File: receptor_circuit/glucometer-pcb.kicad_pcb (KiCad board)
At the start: 2 copper layers, 36.9 x 68.2 mm, 21 parts

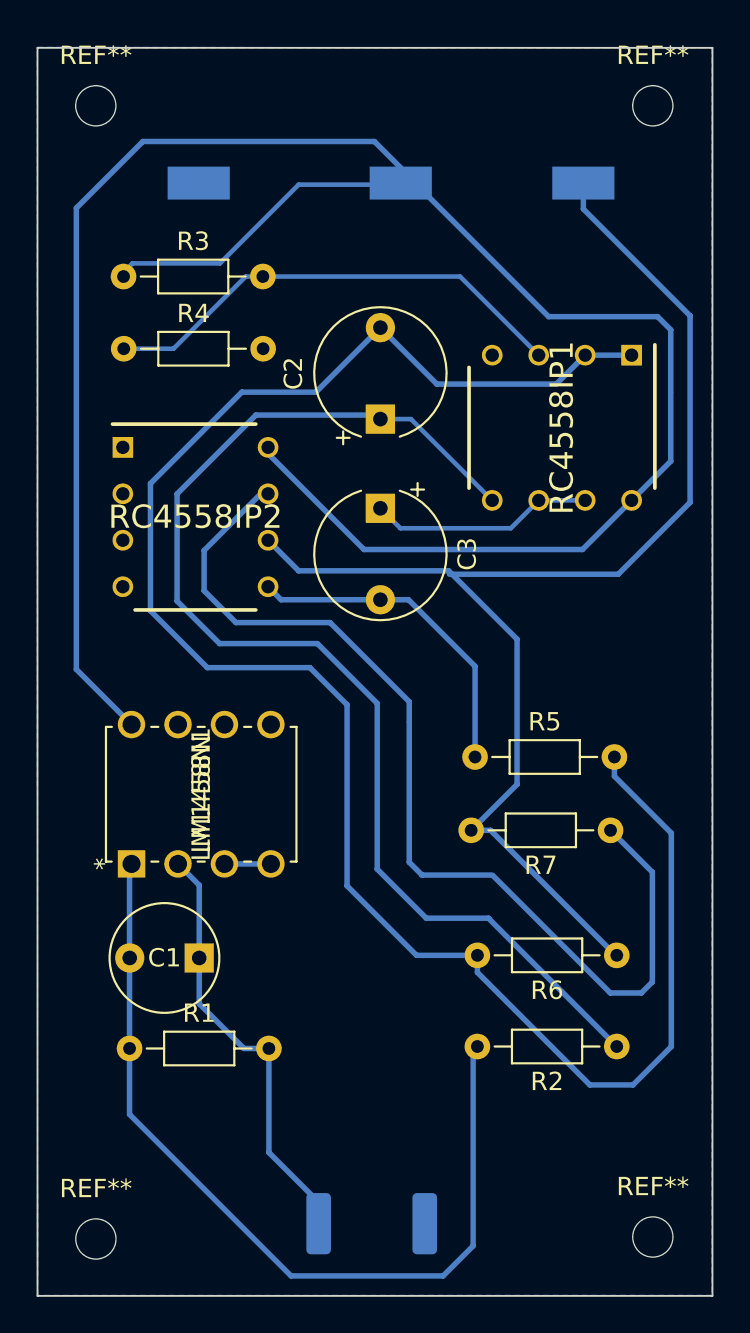
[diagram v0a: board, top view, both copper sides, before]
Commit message: updated footprints
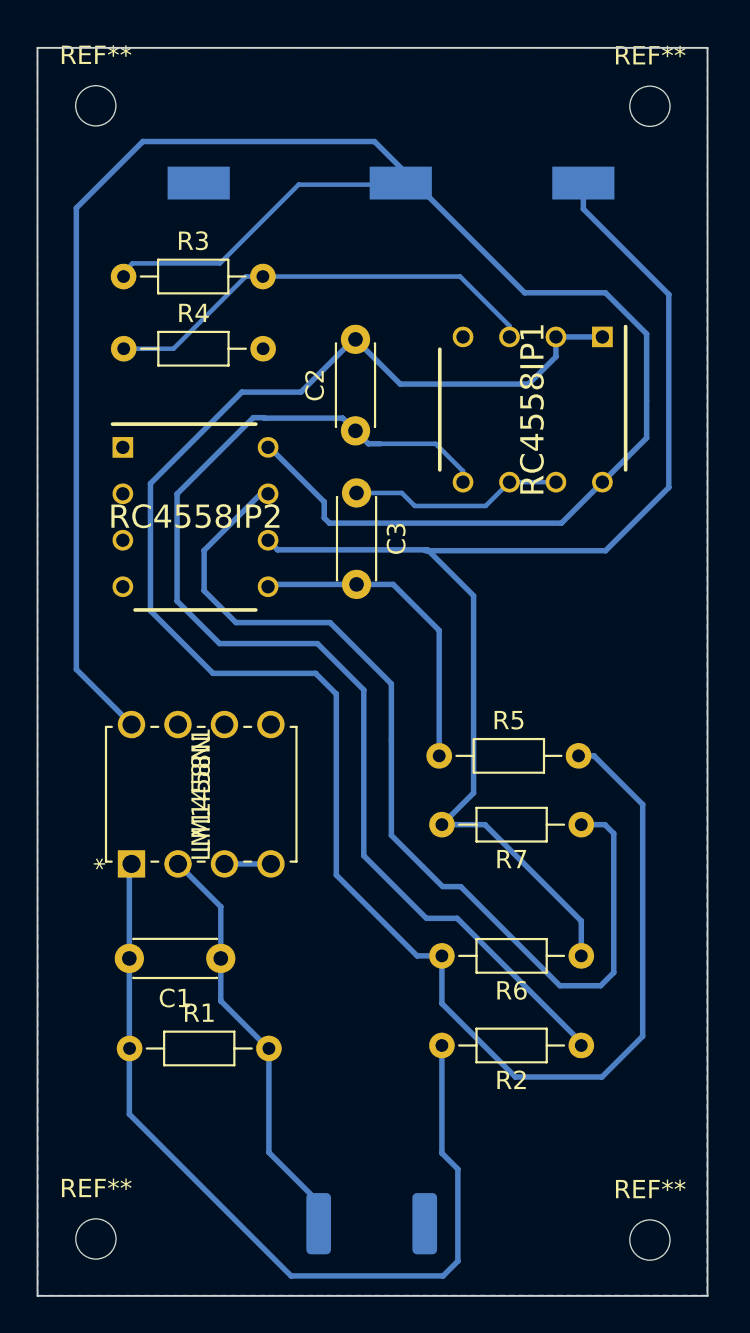
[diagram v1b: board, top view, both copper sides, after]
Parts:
- C1: footprint Capacitor_THT:CP_Radial_D8.0mm_P3.80mm -> Capacitor_THT:C_Disc_D4.3mm_W1.9mm_P5.00mm
- C2, C3: footprint Capacitor_THT:CP_Radial_Tantal_D7.0mm_P5.00mm -> Capacitor_THT:C_Disc_D4.3mm_W1.9mm_P5.00mm
- moved R5 1.96 mm to (194.6, 146.6)
- moved R6 1.94 mm to (202.4, 157.5)
- moved R2 1.94 mm to (202.4, 162.4)
- moved RC4558IP1 1.88 mm to (199.7, 127.7)
- moved R7 1.63 mm to (202.4, 150.4)
- moved C3 1.55 mm to (190.1, 132.2)
- moved C2 1.50 mm to (190.0, 128.8)
- moved C1 1.18 mm to (182.6, 157.7)
- moved REF** 0.23 mm to (206.1, 173.1)
- moved REF** 0.16 mm to (206.1, 111.1)
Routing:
- net VCC: track 119.3 -> 114.9 mm
- net /SIGNAL_1: track 66.4 -> 62.6 mm
- net Net-(R7-Pad1): track 55.5 -> 52.9 mm
- net Net-(R6-Pad1): track 72.7 -> 70.8 mm
- net /PWD_1.65: track 102.4 -> 100.6 mm
- net Net-(R3-Pad2): track 26.1 -> 24.4 mm
- net Net-(C1-Pad1): track 23.7 -> 22.9 mm
- net /SIGNAL_2: track 18.1 -> 17.3 mm
- net Net-(C3-Pad1): track 12.3 -> 11.7 mm
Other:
- board size 36.9 x 68.2 mm -> 36.6 x 68.2 mm

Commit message: updated pcbs
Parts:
- added C10: 15p, Capacitor_THT:C_Disc_D4.3mm_W1.9mm_P5.00mm, F.Cu at (178.8, 66.3)
- added C11: 100n, Capacitor_THT:C_Disc_D4.3mm_W1.9mm_P5.00mm, F.Cu at (186.2, 37.5)
- added C12: 10u, Capacitor_THT:C_Disc_D4.3mm_W1.9mm_P5.00mm, F.Cu at (186.3, 40.9)
- added C13: 15p, Capacitor_THT:C_Disc_D4.3mm_W1.9mm_P5.00mm, F.Cu at (228.8, 66.3)
- added C14: 100n, Capacitor_THT:C_Disc_D4.3mm_W1.9mm_P5.00mm, F.Cu at (236.2, 37.5)
- added C15: 10u, Capacitor_THT:C_Disc_D4.3mm_W1.9mm_P5.00mm, F.Cu at (236.3, 40.9)
- added C16: 15p, Capacitor_THT:C_Disc_D4.3mm_W1.9mm_P5.00mm, F.Cu at (28.8, 146.3)
- added C17: 100n, Capacitor_THT:C_Disc_D4.3mm_W1.9mm_P5.00mm, F.Cu at (36.2, 117.5)
- added C18: 10u, Capacitor_THT:C_Disc_D4.3mm_W1.9mm_P5.00mm, F.Cu at (36.3, 120.9)
- added C19: 15p, Capacitor_THT:C_Disc_D4.3mm_W1.9mm_P5.00mm, F.Cu at (78.8, 146.3)
- added C20: 100n, Capacitor_THT:C_Disc_D4.3mm_W1.9mm_P5.00mm, F.Cu at (86.2, 117.5)
- added C21: 10u, Capacitor_THT:C_Disc_D4.3mm_W1.9mm_P5.00mm, F.Cu at (86.3, 120.9)
- added C22: 15p, Capacitor_THT:C_Disc_D4.3mm_W1.9mm_P5.00mm, F.Cu at (128.8, 146.3)
- added C23: 100n, Capacitor_THT:C_Disc_D4.3mm_W1.9mm_P5.00mm, F.Cu at (136.2, 117.5)
- added C24: 10u, Capacitor_THT:C_Disc_D4.3mm_W1.9mm_P5.00mm, F.Cu at (136.3, 120.9)
- added C25: 15p, Capacitor_THT:C_Disc_D4.3mm_W1.9mm_P5.00mm, F.Cu at (178.8, 146.3)
- added C26: 100n, Capacitor_THT:C_Disc_D4.3mm_W1.9mm_P5.00mm, F.Cu at (186.2, 117.5)
- added C27: 10u, Capacitor_THT:C_Disc_D4.3mm_W1.9mm_P5.00mm, F.Cu at (186.3, 120.9)
- added C28: 15p, Capacitor_THT:C_Disc_D4.3mm_W1.9mm_P5.00mm, F.Cu at (228.8, 146.3)
- added C29: 100n, Capacitor_THT:C_Disc_D4.3mm_W1.9mm_P5.00mm, F.Cu at (236.2, 117.5)
- added C30: 10u, Capacitor_THT:C_Disc_D4.3mm_W1.9mm_P5.00mm, F.Cu at (236.3, 120.9)
- added C4: 15p, Capacitor_THT:C_Disc_D4.3mm_W1.9mm_P5.00mm, F.Cu at (78.8, 66.3)
- added C5: 100n, Capacitor_THT:C_Disc_D4.3mm_W1.9mm_P5.00mm, F.Cu at (86.2, 37.5)
- added C6: 10u, Capacitor_THT:C_Disc_D4.3mm_W1.9mm_P5.00mm, F.Cu at (86.3, 40.9)
- added C7: 15p, Capacitor_THT:C_Disc_D4.3mm_W1.9mm_P5.00mm, F.Cu at (128.8, 66.3)
- added C8: 100n, Capacitor_THT:C_Disc_D4.3mm_W1.9mm_P5.00mm, F.Cu at (136.2, 37.5)
- added C9: 10u, Capacitor_THT:C_Disc_D4.3mm_W1.9mm_P5.00mm, F.Cu at (136.3, 40.9)
- added GND10: TestPoint, TestPoint:TestPoint_Keystone_5015_Micro-Minature, B.Cu at (227.6, 103.9)
- added GND2: TestPoint, TestPoint:TestPoint_Keystone_5015_Micro-Minature, B.Cu at (77.6, 23.9)
- added GND3: TestPoint, TestPoint:TestPoint_Keystone_5015_Micro-Minature, B.Cu at (127.6, 23.9)
- added GND4: TestPoint, TestPoint:TestPoint_Keystone_5015_Micro-Minature, B.Cu at (177.6, 23.9)
- added GND5: TestPoint, TestPoint:TestPoint_Keystone_5015_Micro-Minature, B.Cu at (227.6, 23.9)
- added GND6: TestPoint, TestPoint:TestPoint_Keystone_5015_Micro-Minature, B.Cu at (27.6, 103.9)
- added GND7: TestPoint, TestPoint:TestPoint_Keystone_5015_Micro-Minature, B.Cu at (77.6, 103.9)
- added GND8: TestPoint, TestPoint:TestPoint_Keystone_5015_Micro-Minature, B.Cu at (127.6, 103.9)
- added GND9: TestPoint, TestPoint:TestPoint_Keystone_5015_Micro-Minature, B.Cu at (177.6, 103.9)
- added LM1458N10: LM1458N, Custom:MC1458N, F.Cu at (224.0, 141.1)
- added LM1458N2: LM1458N, Custom:MC1458N, F.Cu at (74.0, 61.1)
- added LM1458N3: LM1458N, Custom:MC1458N, F.Cu at (124.0, 61.1)
- added LM1458N4: LM1458N, Custom:MC1458N, F.Cu at (174.0, 61.1)
- added LM1458N5: LM1458N, Custom:MC1458N, F.Cu at (224.0, 61.1)
- added LM1458N6: LM1458N, Custom:MC1458N, F.Cu at (24.0, 141.1)
- added LM1458N7: LM1458N, Custom:MC1458N, F.Cu at (74.0, 141.1)
- added LM1458N8: LM1458N, Custom:MC1458N, F.Cu at (124.0, 141.1)
- added LM1458N9: LM1458N, Custom:MC1458N, F.Cu at (174.0, 141.1)
- added R10: 10k, Resistor_THT:R_Axial_DIN0204_L3.6mm_D1.6mm_P7.62mm_Horizontal, F.Cu at (73.5, 29.0)
- added R11: 10k, Resistor_THT:R_Axial_DIN0204_L3.6mm_D1.6mm_P7.62mm_Horizontal, F.Cu at (73.5, 33.0)
- added R12: 25k, Resistor_THT:R_Axial_DIN0204_L3.6mm_D1.6mm_P7.62mm_Horizontal, F.Cu at (90.8, 55.2)
- added R13: 1k, Resistor_THT:R_Axial_DIN0204_L3.6mm_D1.6mm_P7.62mm_Horizontal, F.Cu at (98.6, 66.2)
- added R14: 100k, Resistor_THT:R_Axial_DIN0204_L3.6mm_D1.6mm_P7.62mm_Horizontal, F.Cu at (98.6, 59.0)
- added R15: 100k, Resistor_THT:R_Axial_DIN0204_L3.6mm_D1.6mm_P7.62mm_Horizontal, F.Cu at (123.9, 71.2)
- added R16: 330k, Resistor_THT:R_Axial_DIN0204_L3.6mm_D1.6mm_P7.62mm_Horizontal, F.Cu at (148.6, 71.1)
- added R17: 10k, Resistor_THT:R_Axial_DIN0204_L3.6mm_D1.6mm_P7.62mm_Horizontal, F.Cu at (123.5, 29.0)
- added R18: 10k, Resistor_THT:R_Axial_DIN0204_L3.6mm_D1.6mm_P7.62mm_Horizontal, F.Cu at (123.5, 33.0)
- added R19: 25k, Resistor_THT:R_Axial_DIN0204_L3.6mm_D1.6mm_P7.62mm_Horizontal, F.Cu at (140.8, 55.2)
- added R20: 1k, Resistor_THT:R_Axial_DIN0204_L3.6mm_D1.6mm_P7.62mm_Horizontal, F.Cu at (148.6, 66.2)
- added R21: 100k, Resistor_THT:R_Axial_DIN0204_L3.6mm_D1.6mm_P7.62mm_Horizontal, F.Cu at (148.6, 59.0)
- added R22: 100k, Resistor_THT:R_Axial_DIN0204_L3.6mm_D1.6mm_P7.62mm_Horizontal, F.Cu at (173.9, 71.2)
- added R23: 330k, Resistor_THT:R_Axial_DIN0204_L3.6mm_D1.6mm_P7.62mm_Horizontal, F.Cu at (198.6, 71.1)
- added R24: 10k, Resistor_THT:R_Axial_DIN0204_L3.6mm_D1.6mm_P7.62mm_Horizontal, F.Cu at (173.5, 29.0)
- added R25: 10k, Resistor_THT:R_Axial_DIN0204_L3.6mm_D1.6mm_P7.62mm_Horizontal, F.Cu at (173.5, 33.0)
- added R26: 25k, Resistor_THT:R_Axial_DIN0204_L3.6mm_D1.6mm_P7.62mm_Horizontal, F.Cu at (190.8, 55.2)
- added R27: 1k, Resistor_THT:R_Axial_DIN0204_L3.6mm_D1.6mm_P7.62mm_Horizontal, F.Cu at (198.6, 66.2)
- added R28: 100k, Resistor_THT:R_Axial_DIN0204_L3.6mm_D1.6mm_P7.62mm_Horizontal, F.Cu at (198.6, 59.0)
- added R29: 100k, Resistor_THT:R_Axial_DIN0204_L3.6mm_D1.6mm_P7.62mm_Horizontal, F.Cu at (223.9, 71.2)
- added R30: 330k, Resistor_THT:R_Axial_DIN0204_L3.6mm_D1.6mm_P7.62mm_Horizontal, F.Cu at (248.6, 71.1)
- added R31: 10k, Resistor_THT:R_Axial_DIN0204_L3.6mm_D1.6mm_P7.62mm_Horizontal, F.Cu at (223.5, 29.0)
- added R32: 10k, Resistor_THT:R_Axial_DIN0204_L3.6mm_D1.6mm_P7.62mm_Horizontal, F.Cu at (223.5, 33.0)
- added R33: 25k, Resistor_THT:R_Axial_DIN0204_L3.6mm_D1.6mm_P7.62mm_Horizontal, F.Cu at (240.8, 55.2)
- added R34: 1k, Resistor_THT:R_Axial_DIN0204_L3.6mm_D1.6mm_P7.62mm_Horizontal, F.Cu at (248.6, 66.2)
- added R35: 100k, Resistor_THT:R_Axial_DIN0204_L3.6mm_D1.6mm_P7.62mm_Horizontal, F.Cu at (248.6, 59.0)
- added R36: 100k, Resistor_THT:R_Axial_DIN0204_L3.6mm_D1.6mm_P7.62mm_Horizontal, F.Cu at (23.9, 151.2)
- added R37: 330k, Resistor_THT:R_Axial_DIN0204_L3.6mm_D1.6mm_P7.62mm_Horizontal, F.Cu at (48.6, 151.1)
- added R38: 10k, Resistor_THT:R_Axial_DIN0204_L3.6mm_D1.6mm_P7.62mm_Horizontal, F.Cu at (23.5, 109.0)
- added R39: 10k, Resistor_THT:R_Axial_DIN0204_L3.6mm_D1.6mm_P7.62mm_Horizontal, F.Cu at (23.5, 113.0)
- added R40: 25k, Resistor_THT:R_Axial_DIN0204_L3.6mm_D1.6mm_P7.62mm_Horizontal, F.Cu at (40.8, 135.2)
- added R41: 1k, Resistor_THT:R_Axial_DIN0204_L3.6mm_D1.6mm_P7.62mm_Horizontal, F.Cu at (48.6, 146.2)
- added R42: 100k, Resistor_THT:R_Axial_DIN0204_L3.6mm_D1.6mm_P7.62mm_Horizontal, F.Cu at (48.6, 139.0)
- added R43: 100k, Resistor_THT:R_Axial_DIN0204_L3.6mm_D1.6mm_P7.62mm_Horizontal, F.Cu at (73.9, 151.2)
- added R44: 330k, Resistor_THT:R_Axial_DIN0204_L3.6mm_D1.6mm_P7.62mm_Horizontal, F.Cu at (98.6, 151.1)
- added R45: 10k, Resistor_THT:R_Axial_DIN0204_L3.6mm_D1.6mm_P7.62mm_Horizontal, F.Cu at (73.5, 109.0)
- added R46: 10k, Resistor_THT:R_Axial_DIN0204_L3.6mm_D1.6mm_P7.62mm_Horizontal, F.Cu at (73.5, 113.0)
- added R47: 25k, Resistor_THT:R_Axial_DIN0204_L3.6mm_D1.6mm_P7.62mm_Horizontal, F.Cu at (90.8, 135.2)
- added R48: 1k, Resistor_THT:R_Axial_DIN0204_L3.6mm_D1.6mm_P7.62mm_Horizontal, F.Cu at (98.6, 146.2)
- added R49: 100k, Resistor_THT:R_Axial_DIN0204_L3.6mm_D1.6mm_P7.62mm_Horizontal, F.Cu at (98.6, 139.0)
- added R50: 100k, Resistor_THT:R_Axial_DIN0204_L3.6mm_D1.6mm_P7.62mm_Horizontal, F.Cu at (123.9, 151.2)
- added R51: 330k, Resistor_THT:R_Axial_DIN0204_L3.6mm_D1.6mm_P7.62mm_Horizontal, F.Cu at (148.6, 151.1)
- added R52: 10k, Resistor_THT:R_Axial_DIN0204_L3.6mm_D1.6mm_P7.62mm_Horizontal, F.Cu at (123.5, 109.0)
- added R53: 10k, Resistor_THT:R_Axial_DIN0204_L3.6mm_D1.6mm_P7.62mm_Horizontal, F.Cu at (123.5, 113.0)
- added R54: 25k, Resistor_THT:R_Axial_DIN0204_L3.6mm_D1.6mm_P7.62mm_Horizontal, F.Cu at (140.8, 135.2)
- added R55: 1k, Resistor_THT:R_Axial_DIN0204_L3.6mm_D1.6mm_P7.62mm_Horizontal, F.Cu at (148.6, 146.2)
- added R56: 100k, Resistor_THT:R_Axial_DIN0204_L3.6mm_D1.6mm_P7.62mm_Horizontal, F.Cu at (148.6, 139.0)
- added R57: 100k, Resistor_THT:R_Axial_DIN0204_L3.6mm_D1.6mm_P7.62mm_Horizontal, F.Cu at (173.9, 151.2)
- added R58: 330k, Resistor_THT:R_Axial_DIN0204_L3.6mm_D1.6mm_P7.62mm_Horizontal, F.Cu at (198.6, 151.1)
- added R59: 10k, Resistor_THT:R_Axial_DIN0204_L3.6mm_D1.6mm_P7.62mm_Horizontal, F.Cu at (173.5, 109.0)
- added R60: 10k, Resistor_THT:R_Axial_DIN0204_L3.6mm_D1.6mm_P7.62mm_Horizontal, F.Cu at (173.5, 113.0)
- added R61: 25k, Resistor_THT:R_Axial_DIN0204_L3.6mm_D1.6mm_P7.62mm_Horizontal, F.Cu at (190.8, 135.2)
- added R62: 1k, Resistor_THT:R_Axial_DIN0204_L3.6mm_D1.6mm_P7.62mm_Horizontal, F.Cu at (198.6, 146.2)
- added R63: 100k, Resistor_THT:R_Axial_DIN0204_L3.6mm_D1.6mm_P7.62mm_Horizontal, F.Cu at (198.6, 139.0)
- added R64: 100k, Resistor_THT:R_Axial_DIN0204_L3.6mm_D1.6mm_P7.62mm_Horizontal, F.Cu at (223.9, 151.2)
- added R65: 330k, Resistor_THT:R_Axial_DIN0204_L3.6mm_D1.6mm_P7.62mm_Horizontal, F.Cu at (248.6, 151.1)
- added R66: 10k, Resistor_THT:R_Axial_DIN0204_L3.6mm_D1.6mm_P7.62mm_Horizontal, F.Cu at (223.5, 109.0)
- added R67: 10k, Resistor_THT:R_Axial_DIN0204_L3.6mm_D1.6mm_P7.62mm_Horizontal, F.Cu at (223.5, 113.0)
- added R68: 25k, Resistor_THT:R_Axial_DIN0204_L3.6mm_D1.6mm_P7.62mm_Horizontal, F.Cu at (240.8, 135.2)
- added R69: 1k, Resistor_THT:R_Axial_DIN0204_L3.6mm_D1.6mm_P7.62mm_Horizontal, F.Cu at (248.6, 146.2)
- added R70: 100k, Resistor_THT:R_Axial_DIN0204_L3.6mm_D1.6mm_P7.62mm_Horizontal, F.Cu at (248.6, 139.0)
- added R8: 100k, Resistor_THT:R_Axial_DIN0204_L3.6mm_D1.6mm_P7.62mm_Horizontal, F.Cu at (73.9, 71.2)
- added R9: 330k, Resistor_THT:R_Axial_DIN0204_L3.6mm_D1.6mm_P7.62mm_Horizontal, F.Cu at (98.6, 71.1)
- added RC4558IP10: RC4558IP, Custom:DIP794W53P254L959H508Q8N, F.Cu at (227.5, 42.2)
- added RC4558IP11: RC4558IP, Custom:DIP794W53P254L959H508Q8N, F.Cu at (45.9, 116.3)
- added RC4558IP12: RC4558IP, Custom:DIP794W53P254L959H508Q8N, F.Cu at (27.5, 122.2)
- added RC4558IP13: RC4558IP, Custom:DIP794W53P254L959H508Q8N, F.Cu at (95.9, 116.3)
- added RC4558IP14: RC4558IP, Custom:DIP794W53P254L959H508Q8N, F.Cu at (77.5, 122.2)
- added RC4558IP15: RC4558IP, Custom:DIP794W53P254L959H508Q8N, F.Cu at (145.9, 116.3)
- added RC4558IP16: RC4558IP, Custom:DIP794W53P254L959H508Q8N, F.Cu at (127.5, 122.2)
- added RC4558IP17: RC4558IP, Custom:DIP794W53P254L959H508Q8N, F.Cu at (195.9, 116.3)
- added RC4558IP18: RC4558IP, Custom:DIP794W53P254L959H508Q8N, F.Cu at (177.5, 122.2)
- added RC4558IP19: RC4558IP, Custom:DIP794W53P254L959H508Q8N, F.Cu at (245.9, 116.3)
- added RC4558IP20: RC4558IP, Custom:DIP794W53P254L959H508Q8N, F.Cu at (227.5, 122.2)
- added RC4558IP3: RC4558IP, Custom:DIP794W53P254L959H508Q8N, F.Cu at (95.9, 36.3)
- added RC4558IP4: RC4558IP, Custom:DIP794W53P254L959H508Q8N, F.Cu at (77.5, 42.2)
- added RC4558IP5: RC4558IP, Custom:DIP794W53P254L959H508Q8N, F.Cu at (145.9, 36.3)
- added RC4558IP6: RC4558IP, Custom:DIP794W53P254L959H508Q8N, F.Cu at (127.5, 42.2)
- added RC4558IP7: RC4558IP, Custom:DIP794W53P254L959H508Q8N, F.Cu at (195.9, 36.3)
- added RC4558IP8: RC4558IP, Custom:DIP794W53P254L959H508Q8N, F.Cu at (177.5, 42.2)
- added RC4558IP9: RC4558IP, Custom:DIP794W53P254L959H508Q8N, F.Cu at (245.9, 36.3)
- added RECEPTOR_DIODE10: D_Photo, LED_SMD:LED_2512_6332Metric, B.Cu at (237.1, 160.8)
- added RECEPTOR_DIODE2: D_Photo, LED_SMD:LED_2512_6332Metric, B.Cu at (87.1, 80.8)
- added RECEPTOR_DIODE3: D_Photo, LED_SMD:LED_2512_6332Metric, B.Cu at (137.1, 80.8)
- added RECEPTOR_DIODE4: D_Photo, LED_SMD:LED_2512_6332Metric, B.Cu at (187.1, 80.8)
- added RECEPTOR_DIODE5: D_Photo, LED_SMD:LED_2512_6332Metric, B.Cu at (237.1, 80.8)
- added RECEPTOR_DIODE6: D_Photo, LED_SMD:LED_2512_6332Metric, B.Cu at (37.1, 160.8)
- added RECEPTOR_DIODE7: D_Photo, LED_SMD:LED_2512_6332Metric, B.Cu at (87.1, 160.8)
- added RECEPTOR_DIODE8: D_Photo, LED_SMD:LED_2512_6332Metric, B.Cu at (137.1, 160.8)
- added RECEPTOR_DIODE9: D_Photo, LED_SMD:LED_2512_6332Metric, B.Cu at (187.1, 160.8)
- added REF**1: MountingHole_2.2mm_M2_ISO7380, MountingHole:MountingHole_2.2mm_M2_ISO7380, F.Cu at (102.3, 81.7)
- added REF**10: MountingHole_2.2mm_M2_ISO7380, MountingHole:MountingHole_2.2mm_M2_ISO7380, F.Cu at (172.0, 81.6)
- added REF**11: MountingHole_2.2mm_M2_ISO7380, MountingHole:MountingHole_2.2mm_M2_ISO7380, F.Cu at (202.3, 19.7)
- added REF**12: MountingHole_2.2mm_M2_ISO7380, MountingHole:MountingHole_2.2mm_M2_ISO7380, F.Cu at (172.0, 19.7)
- added REF**13: MountingHole_2.2mm_M2_ISO7380, MountingHole:MountingHole_2.2mm_M2_ISO7380, F.Cu at (252.3, 81.7)
- added REF**14: MountingHole_2.2mm_M2_ISO7380, MountingHole:MountingHole_2.2mm_M2_ISO7380, F.Cu at (222.0, 81.6)
- added REF**15: MountingHole_2.2mm_M2_ISO7380, MountingHole:MountingHole_2.2mm_M2_ISO7380, F.Cu at (252.3, 19.7)
- added REF**16: MountingHole_2.2mm_M2_ISO7380, MountingHole:MountingHole_2.2mm_M2_ISO7380, F.Cu at (222.0, 19.7)
- added REF**17: MountingHole_2.2mm_M2_ISO7380, MountingHole:MountingHole_2.2mm_M2_ISO7380, F.Cu at (52.3, 161.7)
- added REF**18: MountingHole_2.2mm_M2_ISO7380, MountingHole:MountingHole_2.2mm_M2_ISO7380, F.Cu at (22.0, 161.6)
- added REF**19: MountingHole_2.2mm_M2_ISO7380, MountingHole:MountingHole_2.2mm_M2_ISO7380, F.Cu at (52.3, 99.7)
- added REF**2: MountingHole_2.2mm_M2_ISO7380, MountingHole:MountingHole_2.2mm_M2_ISO7380, F.Cu at (72.0, 81.6)
- added REF**20: MountingHole_2.2mm_M2_ISO7380, MountingHole:MountingHole_2.2mm_M2_ISO7380, F.Cu at (22.0, 99.7)
- added REF**21: MountingHole_2.2mm_M2_ISO7380, MountingHole:MountingHole_2.2mm_M2_ISO7380, F.Cu at (102.3, 161.7)
- added REF**22: MountingHole_2.2mm_M2_ISO7380, MountingHole:MountingHole_2.2mm_M2_ISO7380, F.Cu at (72.0, 161.6)
- added REF**23: MountingHole_2.2mm_M2_ISO7380, MountingHole:MountingHole_2.2mm_M2_ISO7380, F.Cu at (102.3, 99.7)
- added REF**24: MountingHole_2.2mm_M2_ISO7380, MountingHole:MountingHole_2.2mm_M2_ISO7380, F.Cu at (72.0, 99.7)
- added REF**25: MountingHole_2.2mm_M2_ISO7380, MountingHole:MountingHole_2.2mm_M2_ISO7380, F.Cu at (152.3, 161.7)
- added REF**26: MountingHole_2.2mm_M2_ISO7380, MountingHole:MountingHole_2.2mm_M2_ISO7380, F.Cu at (122.0, 161.6)
- added REF**27: MountingHole_2.2mm_M2_ISO7380, MountingHole:MountingHole_2.2mm_M2_ISO7380, F.Cu at (152.3, 99.7)
- added REF**28: MountingHole_2.2mm_M2_ISO7380, MountingHole:MountingHole_2.2mm_M2_ISO7380, F.Cu at (122.0, 99.7)
- added REF**29: MountingHole_2.2mm_M2_ISO7380, MountingHole:MountingHole_2.2mm_M2_ISO7380, F.Cu at (202.3, 161.7)
- added REF**3: MountingHole_2.2mm_M2_ISO7380, MountingHole:MountingHole_2.2mm_M2_ISO7380, F.Cu at (102.3, 19.7)
- added REF**30: MountingHole_2.2mm_M2_ISO7380, MountingHole:MountingHole_2.2mm_M2_ISO7380, F.Cu at (172.0, 161.6)
- added REF**31: MountingHole_2.2mm_M2_ISO7380, MountingHole:MountingHole_2.2mm_M2_ISO7380, F.Cu at (202.3, 99.7)
- added REF**32: MountingHole_2.2mm_M2_ISO7380, MountingHole:MountingHole_2.2mm_M2_ISO7380, F.Cu at (172.0, 99.7)
- added REF**33: MountingHole_2.2mm_M2_ISO7380, MountingHole:MountingHole_2.2mm_M2_ISO7380, F.Cu at (252.3, 161.7)
- added REF**34: MountingHole_2.2mm_M2_ISO7380, MountingHole:MountingHole_2.2mm_M2_ISO7380, F.Cu at (222.0, 161.6)
- added REF**35: MountingHole_2.2mm_M2_ISO7380, MountingHole:MountingHole_2.2mm_M2_ISO7380, F.Cu at (252.3, 99.7)
- added REF**36: MountingHole_2.2mm_M2_ISO7380, MountingHole:MountingHole_2.2mm_M2_ISO7380, F.Cu at (222.0, 99.7)
- added REF**4: MountingHole_2.2mm_M2_ISO7380, MountingHole:MountingHole_2.2mm_M2_ISO7380, F.Cu at (72.0, 19.7)
- added REF**5: MountingHole_2.2mm_M2_ISO7380, MountingHole:MountingHole_2.2mm_M2_ISO7380, F.Cu at (152.3, 81.7)
- added REF**6: MountingHole_2.2mm_M2_ISO7380, MountingHole:MountingHole_2.2mm_M2_ISO7380, F.Cu at (122.0, 81.6)
- added REF**7: MountingHole_2.2mm_M2_ISO7380, MountingHole:MountingHole_2.2mm_M2_ISO7380, F.Cu at (152.3, 19.7)
- added REF**8: MountingHole_2.2mm_M2_ISO7380, MountingHole:MountingHole_2.2mm_M2_ISO7380, F.Cu at (122.0, 19.7)
- added REF**9: MountingHole_2.2mm_M2_ISO7380, MountingHole:MountingHole_2.2mm_M2_ISO7380, F.Cu at (202.3, 81.7)
- added S_OUT10: SIGNAL_OUT, TestPoint:TestPoint_Keystone_5015_Micro-Minature, B.Cu at (248.7, 103.9)
- added S_OUT2: SIGNAL_OUT, TestPoint:TestPoint_Keystone_5015_Micro-Minature, B.Cu at (98.7, 23.9)
- added S_OUT3: SIGNAL_OUT, TestPoint:TestPoint_Keystone_5015_Micro-Minature, B.Cu at (148.7, 23.9)
- added S_OUT4: SIGNAL_OUT, TestPoint:TestPoint_Keystone_5015_Micro-Minature, B.Cu at (198.7, 23.9)
- added S_OUT5: SIGNAL_OUT, TestPoint:TestPoint_Keystone_5015_Micro-Minature, B.Cu at (248.7, 23.9)
- added S_OUT6: SIGNAL_OUT, TestPoint:TestPoint_Keystone_5015_Micro-Minature, B.Cu at (48.7, 103.9)
- added S_OUT7: SIGNAL_OUT, TestPoint:TestPoint_Keystone_5015_Micro-Minature, B.Cu at (98.7, 103.9)
- added S_OUT8: SIGNAL_OUT, TestPoint:TestPoint_Keystone_5015_Micro-Minature, B.Cu at (148.7, 103.9)
- added S_OUT9: SIGNAL_OUT, TestPoint:TestPoint_Keystone_5015_Micro-Minature, B.Cu at (198.7, 103.9)
- added VCC10: TestPoint, TestPoint:TestPoint_Keystone_5015_Micro-Minature, B.Cu at (238.7, 103.9)
- added VCC2: TestPoint, TestPoint:TestPoint_Keystone_5015_Micro-Minature, B.Cu at (88.7, 23.9)
- added VCC3: TestPoint, TestPoint:TestPoint_Keystone_5015_Micro-Minature, B.Cu at (138.7, 23.9)
- added VCC4: TestPoint, TestPoint:TestPoint_Keystone_5015_Micro-Minature, B.Cu at (188.7, 23.9)
- added VCC5: TestPoint, TestPoint:TestPoint_Keystone_5015_Micro-Minature, B.Cu at (238.7, 23.9)
- added VCC6: TestPoint, TestPoint:TestPoint_Keystone_5015_Micro-Minature, B.Cu at (38.7, 103.9)
- added VCC7: TestPoint, TestPoint:TestPoint_Keystone_5015_Micro-Minature, B.Cu at (88.7, 103.9)
- added VCC8: TestPoint, TestPoint:TestPoint_Keystone_5015_Micro-Minature, B.Cu at (138.7, 103.9)
- added VCC9: TestPoint, TestPoint:TestPoint_Keystone_5015_Micro-Minature, B.Cu at (188.7, 103.9)
- moved R1 178.9 mm to (23.9, 71.2)
- moved VCC1 178.9 mm to (38.7, 23.9)
- moved C1 178.9 mm to (28.8, 66.3)
- moved C2 178.9 mm to (36.2, 37.5)
- moved C3 178.9 mm to (36.3, 40.9)
- moved GND1 178.9 mm to (27.6, 23.9)
- moved LM1458N1 178.9 mm to (24.0, 61.1)
- moved R2 178.9 mm to (48.6, 71.1)
- moved R3 178.9 mm to (23.5, 29.0)
- moved R4 178.9 mm to (23.5, 33.0)
- moved R5 178.9 mm to (40.8, 55.2)
- moved R6 178.9 mm to (48.6, 66.2)
- moved R7 178.9 mm to (48.6, 59.0)
- moved RC4558IP1 178.9 mm to (45.9, 36.3)
- moved RC4558IP2 178.9 mm to (27.5, 42.2)
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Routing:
- net VCC: track 114.9 -> 1149.3 mm
- net /PWD_1.65: track 100.6 -> 1006.4 mm
- net Net-(R6-Pad1): track 70.8 -> 707.6 mm
- net /SIGNAL_1: track 62.6 -> 625.7 mm
- net Net-(R7-Pad1): track 52.9 -> 529.2 mm
- net Net-(C1-Pad2): track 47.8 -> 478.5 mm
- net Net-(R3-Pad2): track 24.4 -> 244.5 mm
- net Net-(C1-Pad1): track 22.9 -> 228.7 mm
- net /SIGNAL_2: track 17.3 -> 173.1 mm
- net Net-(C3-Pad1): track 11.7 -> 117.4 mm
- net GND: track 3.16 -> 31.6 mm
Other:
- board size 36.6 x 68.2 mm -> 236.6 x 148.2 mm

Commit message: added prints
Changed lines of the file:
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@@
     (pad_to_mask_clearance 0)
     (pcbplotparams
-      (layerselection 0x00010fc_ffffffff)
+      (layerselection 0x0000000_fffffffe)
       (disableapertmacros false)
       (usegerberextensions false)
@@
       (svguseinch false)
       (svgprecision 6)
-      (excludeedgelayer true)
+      (excludeedgelayer false)
       (plotframeref false)
       (viasonmask false)
@@
       (dxfimperialunits true)
       (dxfusepcbnewfont true)
-      (psnegative false)
+      (psnegative true)
       (psa4output false)
-      (plotreference true)
-      (plotvalue true)
+      (plotreference false)
+      (plotvalue false)
       (plotinvisibletext false)
       (sketchpadsonfab false)
       (subtractmaskfromsilk false)
-      (outputformat 1)
+      (outputformat 4)
       (mirror false)
       (drillshape 1)
       (scaleselection 1)
-      (outputdirectory "")
+      (outputdirectory "../ready-to-print/")
     )
   )
@@
     (fp_line (start 3.15 1.6) (end -2.35 1.6) (layer "B.Fab") (width 0.1))
     (fp_line (start -3.15 -1.6) (end 3.15 -1.6) (layer "B.Fab") (width 0.1))
-    (pad "1" smd roundrect (at -2.9 0 180) (size 1.35 3.35) (layers "B.Cu" "B.Paste" "B.Mask") (roundrect_rratio 0.185185)
+    (pad "1" smd roundrect (at -2.9 0 180) (size 1.35 3.35) (layers "B.Cu" "B.Paste" "B.Mask") (roundrect_rratio 0.1851851852)
       (net 8 "GND") (pinfunction "K") (pintype "passive"))
-    (pad "2" smd roundrect (at 2.9 0 180) (size 1.35 3.35) (layers "B.Cu" "B.Paste" "B.Mask") (roundrect_rratio 0.185185)
+    (pad "2" smd roundrect (at 2.9 0 180) (size 1.35 3.35) (layers "B.Cu" "B.Paste" "B.Mask") (roundrect_rratio 0.1851851852)
       (net 1 "Net-(C1-Pad1)") (pinfunction "A") (pintype "passive"))
     (model "${KICAD6_3DMODEL_DIR}/LED_SMD.3dshapes/LED_2512_6332Metric.wrl"
@@
     (fp_line (start 3.15 1.6) (end -2.35 1.6) (layer "B.Fab") (width 0.1))
     (fp_line (start -3.15 -1.6) (end 3.15 -1.6) (layer "B.Fab") (width 0.1))
-    (pad "1" smd roundrect (at -2.9 0 180) (size 1.35 3.35) (layers "B.Cu" "B.Paste" "B.Mask") (roundrect_rratio 0.185185)
+    (pad "1" smd roundrect (at -2.9 0 180) (size 1.35 3.35) (layers "B.Cu" "B.Paste" "B.Mask") (roundrect_rratio 0.1851851852)
       (net 8 "GND") (pinfunction "K") (pintype "passive"))
-    (pad "2" smd roundrect (at 2.9 0 180) (size 1.35 3.35) (layers "B.Cu" "B.Paste" "B.Mask") (roundrect_rratio 0.185185)
+    (pad "2" smd roundrect (at 2.9 0 180) (size 1.35 3.35) (layers "B.Cu" "B.Paste" "B.Mask") (roundrect_rratio 0.1851851852)
       (net 1 "Net-(C1-Pad1)") (pinfunction "A") (pintype "passive"))
     (model "${KICAD6_3DMODEL_DIR}/LED_SMD.3dshapes/LED_2512_6332Metric.wrl"
@@
     (fp_line (start 3.15 -1.6) (end 3.15 1.6) (layer "B.Fab") (width 0.1))
     (fp_line (start -2.35 1.6) (end -3.15 0.8) (layer "B.Fab") (width 0.1))
-    (pad "1" smd roundrect (at -2.9 0 180) (size 1.35 3.35) (layers "B.Cu" "B.Paste" "B.Mask") (roundrect_rratio 0.185185)
+    (pad "1" smd roundrect (at -2.9 0 180) (size 1.35 3.35) (layers "B.Cu" "B.Paste" "B.Mask") (roundrect_rratio 0.1851851852)
       (net 8 "GND") (pinfunction "K") (pintype "passive"))
-    (pad "2" smd roundrect (at 2.9 0 180) (size 1.35 3.35) (layers "B.Cu" "B.Paste" "B.Mask") (roundrect_rratio 0.185185)
+    (pad "2" smd roundrect (at 2.9 0 180) (size 1.35 3.35) (layers "B.Cu" "B.Paste" "B.Mask") (roundrect_rratio 0.1851851852)
       (net 1 "Net-(C1-Pad1)") (pinfunction "A") (pintype "passive"))
     (model "${KICAD6_3DMODEL_DIR}/LED_SMD.3dshapes/LED_2512_6332Metric.wrl"
@@
     (fp_line (start -2.35 1.6) (end -3.15 0.8) (layer "B.Fab") (width 0.1))
     (fp_line (start 3.15 1.6) (end -2.35 1.6) (layer "B.Fab") (width 0.1))
-    (pad "1" smd roundrect (at -2.9 0 180) (size 1.35 3.35) (layers "B.Cu" "B.Paste" "B.Mask") (roundrect_rratio 0.185185)
+    (pad "1" smd roundrect (at -2.9 0 180) (size 1.35 3.35) (layers "B.Cu" "B.Paste" "B.Mask") (roundrect_rratio 0.1851851852)
       (net 8 "GND") (pinfunction "K") (pintype "passive"))
-    (pad "2" smd roundrect (at 2.9 0 180) (size 1.35 3.35) (layers "B.Cu" "B.Paste" "B.Mask") (roundrect_rratio 0.185185)
+    (pad "2" smd roundrect (at 2.9 0 180) (size 1.35 3.35) (layers "B.Cu" "B.Paste" "B.Mask") (roundrect_rratio 0.1851851852)
       (net 1 "Net-(C1-Pad1)") (pinfunction "A") (pintype "passive"))
     (model "${KICAD6_3DMODEL_DIR}/LED_SMD.3dshapes/LED_2512_6332Metric.wrl"
@@
     (fp_line (start -3.15 0.8) (end -3.15 -1.6) (layer "B.Fab") (width 0.1))
     (fp_line (start 3.15 -1.6) (end 3.15 1.6) (layer "B.Fab") (width 0.1))
-    (pad "1" smd roundrect (at -2.9 0 180) (size 1.35 3.35) (layers "B.Cu" "B.Paste" "B.Mask") (roundrect_rratio 0.185185)
+    (pad "1" smd roundrect (at -2.9 0 180) (size 1.35 3.35) (layers "B.Cu" "B.Paste" "B.Mask") (roundrect_rratio 0.1851851852)
       (net 8 "GND") (pinfunction "K") (pintype "passive"))
-    (pad "2" smd roundrect (at 2.9 0 180) (size 1.35 3.35) (layers "B.Cu" "B.Paste" "B.Mask") (roundrect_rratio 0.185185)
+    (pad "2" smd roundrect (at 2.9 0 180) (size 1.35 3.35) (layers "B.Cu" "B.Paste" "B.Mask") (roundrect_rratio 0.1851851852)
       (net 1 "Net-(C1-Pad1)") (pinfunction "A") (pintype "passive"))
     (model "${KICAD6_3DMODEL_DIR}/LED_SMD.3dshapes/LED_2512_6332Metric.wrl"
@@
     (fp_line (start -3.15 0.8) (end -3.15 -1.6) (layer "B.Fab") (width 0.1))
     (fp_line (start 3.15 -1.6) (end 3.15 1.6) (layer "B.Fab") (width 0.1))
-    (pad "1" smd roundrect (at -2.9 0 180) (size 1.35 3.35) (layers "B.Cu" "B.Paste" "B.Mask") (roundrect_rratio 0.185185)
+    (pad "1" smd roundrect (at -2.9 0 180) (size 1.35 3.35) (layers "B.Cu" "B.Paste" "B.Mask") (roundrect_rratio 0.1851851852)
       (net 8 "GND") (pinfunction "K") (pintype "passive"))
-    (pad "2" smd roundrect (at 2.9 0 180) (size 1.35 3.35) (layers "B.Cu" "B.Paste" "B.Mask") (roundrect_rratio 0.185185)
+    (pad "2" smd roundrect (at 2.9 0 180) (size 1.35 3.35) (layers "B.Cu" "B.Paste" "B.Mask") (roundrect_rratio 0.1851851852)
       (net 1 "Net-(C1-Pad1)") (pinfunction "A") (pintype "passive"))
     (model "${KICAD6_3DMODEL_DIR}/LED_SMD.3dshapes/LED_2512_6332Metric.wrl"
@@
     (fp_line (start 3.15 1.6) (end -2.35 1.6) (layer "B.Fab") (width 0.1))
     (fp_line (start -3.15 0.8) (end -3.15 -1.6) (layer "B.Fab") (width 0.1))
-    (pad "1" smd roundrect (at -2.9 0 180) (size 1.35 3.35) (layers "B.Cu" "B.Paste" "B.Mask") (roundrect_rratio 0.185185)
+    (pad "1" smd roundrect (at -2.9 0 180) (size 1.35 3.35) (layers "B.Cu" "B.Paste" "B.Mask") (roundrect_rratio 0.1851851852)
       (net 8 "GND") (pinfunction "K") (pintype "passive"))
-    (pad "2" smd roundrect (at 2.9 0 180) (size 1.35 3.35) (layers "B.Cu" "B.Paste" "B.Mask") (roundrect_rratio 0.185185)
+    (pad "2" smd roundrect (at 2.9 0 180) (size 1.35 3.35) (layers "B.Cu" "B.Paste" "B.Mask") (roundrect_rratio 0.1851851852)
       (net 1 "Net-(C1-Pad1)") (pinfunction "A") (pintype "passive"))
     (model "${KICAD6_3DMODEL_DIR}/LED_SMD.3dshapes/LED_2512_6332Metric.wrl"
@@
     (fp_line (start -3.15 -1.6) (end 3.15 -1.6) (layer "B.Fab") (width 0.1))
     (fp_line (start 3.15 1.6) (end -2.35 1.6) (layer "B.Fab") (width 0.1))
-    (pad "1" smd roundrect (at -2.9 0 180) (size 1.35 3.35) (layers "B.Cu" "B.Paste" "B.Mask") (roundrect_rratio 0.185185)
+    (pad "1" smd roundrect (at -2.9 0 180) (size 1.35 3.35) (layers "B.Cu" "B.Paste" "B.Mask") (roundrect_rratio 0.1851851852)
       (net 8 "GND") (pinfunction "K") (pintype "passive"))
-    (pad "2" smd roundrect (at 2.9 0 180) (size 1.35 3.35) (layers "B.Cu" "B.Paste" "B.Mask") (roundrect_rratio 0.185185)
+    (pad "2" smd roundrect (at 2.9 0 180) (size 1.35 3.35) (layers "B.Cu" "B.Paste" "B.Mask") (roundrect_rratio 0.1851851852)
       (net 1 "Net-(C1-Pad1)") (pinfunction "A") (pintype "passive"))
     (model "${KICAD6_3DMODEL_DIR}/LED_SMD.3dshapes/LED_2512_6332Metric.wrl"
@@
     (fp_line (start -2.35 1.6) (end -3.15 0.8) (layer "B.Fab") (width 0.1))
     (fp_line (start 3.15 -1.6) (end 3.15 1.6) (layer "B.Fab") (width 0.1))
-    (pad "1" smd roundrect (at -2.9 0 180) (size 1.35 3.35) (layers "B.Cu" "B.Paste" "B.Mask") (roundrect_rratio 0.185185)
+    (pad "1" smd roundrect (at -2.9 0 180) (size 1.35 3.35) (layers "B.Cu" "B.Paste" "B.Mask") (roundrect_rratio 0.1851851852)
       (net 8 "GND") (pinfunction "K") (pintype "passive"))
-    (pad "2" smd roundrect (at 2.9 0 180) (size 1.35 3.35) (layers "B.Cu" "B.Paste" "B.Mask") (roundrect_rratio 0.185185)
+    (pad "2" smd roundrect (at 2.9 0 180) (size 1.35 3.35) (layers "B.Cu" "B.Paste" "B.Mask") (roundrect_rratio 0.1851851852)
       (net 1 "Net-(C1-Pad1)") (pinfunction "A") (pintype "passive"))
     (model "${KICAD6_3DMODEL_DIR}/LED_SMD.3dshapes/LED_2512_6332Metric.wrl"
@@
     (fp_line (start 3.15 -1.6) (end 3.15 1.6) (layer "B.Fab") (width 0.1))
     (fp_line (start -3.15 -1.6) (end 3.15 -1.6) (layer "B.Fab") (width 0.1))
-    (pad "1" smd roundrect (at -2.9 0 180) (size 1.35 3.35) (layers "B.Cu" "B.Paste" "B.Mask") (roundrect_rratio 0.185185)
+    (pad "1" smd roundrect (at -2.9 0 180) (size 1.35 3.35) (layers "B.Cu" "B.Paste" "B.Mask") (roundrect_rratio 0.1851851852)
       (net 8 "GND") (pinfunction "K") (pintype "passive"))
-    (pad "2" smd roundrect (at 2.9 0 180) (size 1.35 3.35) (layers "B.Cu" "B.Paste" "B.Mask") (roundrect_rratio 0.185185)
+    (pad "2" smd roundrect (at 2.9 0 180) (size 1.35 3.35) (layers "B.Cu" "B.Paste" "B.Mask") (roundrect_rratio 0.1851851852)
       (net 1 "Net-(C1-Pad1)") (pinfunction "A") (pintype "passive"))
     (model "${KICAD6_3DMODEL_DIR}/LED_SMD.3dshapes/LED_2512_6332Metric.wrl"
